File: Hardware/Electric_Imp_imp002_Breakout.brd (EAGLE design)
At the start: 43.2 x 45.7 mm, 41 parts, among them Q1 DMG2307L-7, Q2 PHOTOTRANSISTORPT17-21C-L41-T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, U1 imp002, U2 TPS62172, X1 USBSMD

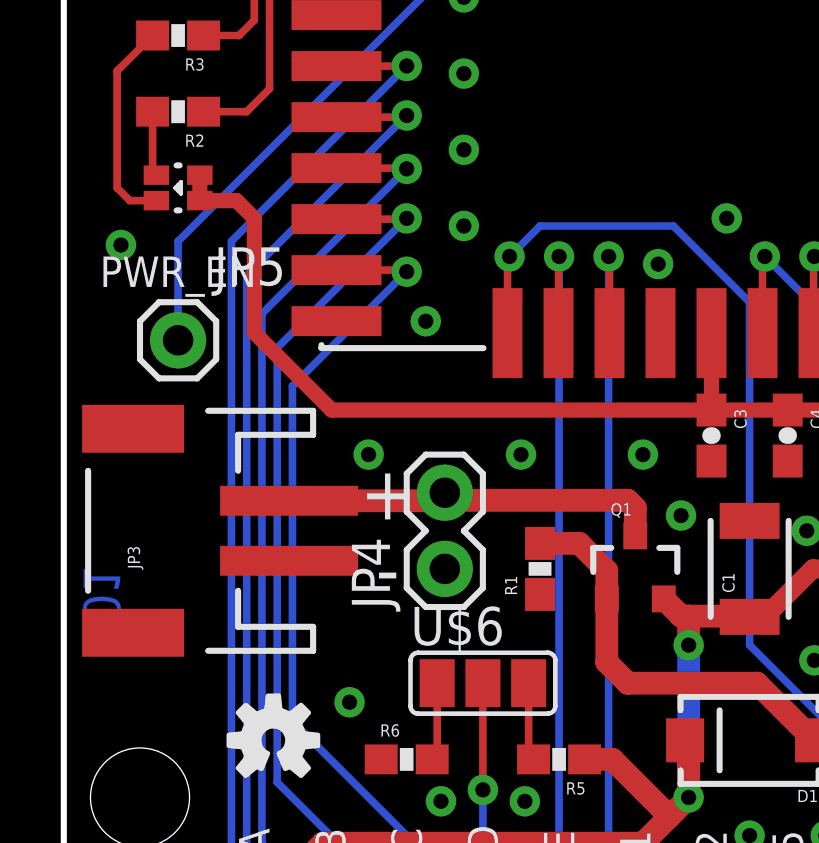
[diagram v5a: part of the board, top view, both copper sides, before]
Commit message: Added silk to the 3-way jumper, moved marking for dual-color diode to outside footprint, and changed phototransistor gain resistor to 33k
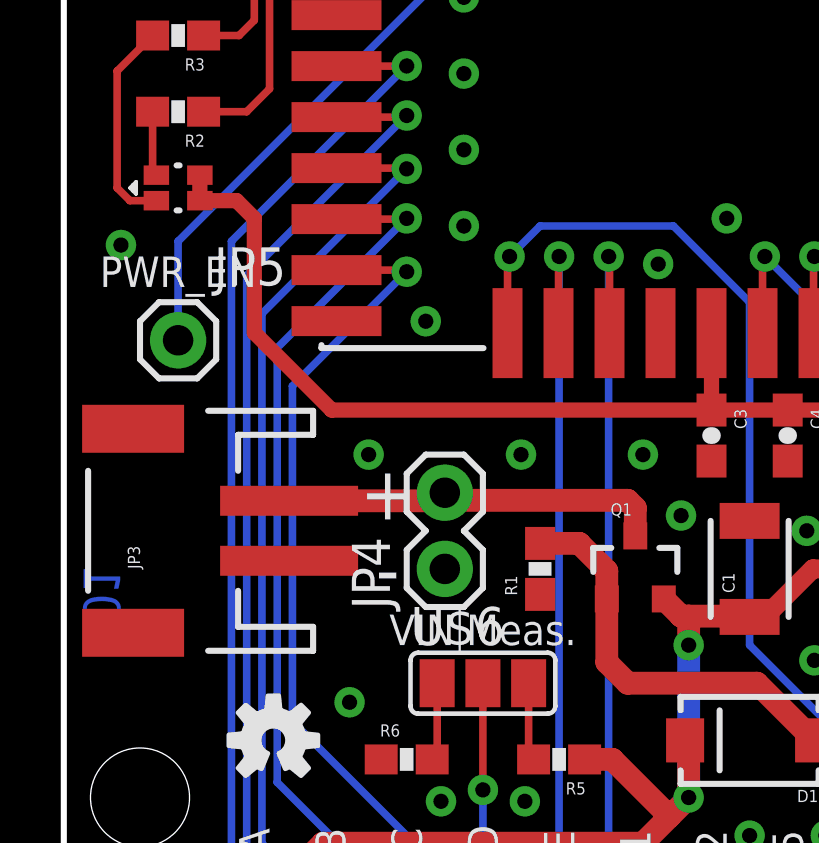
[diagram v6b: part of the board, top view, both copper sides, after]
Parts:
- R4: value 62k -> 33k
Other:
- board text added: "VIN Meas."
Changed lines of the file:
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@@
 <setting verticaltext="up"/>
 </settings>
-<grid distance="0.05" unitdist="inch" unit="inch" style="dots" multiple="1" display="yes" altdistance="0.005" altunitdist="inch" altunit="inch"/>
+<grid distance="0.01" unitdist="inch" unit="inch" style="dots" multiple="1" display="yes" altdistance="0.005" altunitdist="inch" altunit="inch"/>
 <layers>
 <layer number="1" name="Top" color="4" fill="1" visible="yes" active="yes"/>
 <layer number="2" name="Route2" color="1" fill="3" visible="no" active="yes"/>
 <layer number="15" name="Route15" color="4" fill="6" visible="no" active="yes"/>
-<layer number="16" name="Bottom" color="1" fill="1" visible="yes" active="yes"/>
+<layer number="16" name="Bottom" color="1" fill="1" visible="no" active="yes"/>
 <layer number="17" name="Pads" color="2" fill="1" visible="yes" active="yes"/>
 <layer number="18" name="Vias" color="2" fill="1" visible="yes" active="yes"/>
@@
 <layer number="20" name="Dimension" color="15" fill="1" visible="yes" active="yes"/>
 <layer number="21" name="tPlace" color="16" fill="1" visible="yes" active="yes"/>
-<layer number="22" name="bPlace" color="14" fill="1" visible="yes" active="yes"/>
+<layer number="22" name="bPlace" color="14" fill="1" visible="no" active="yes"/>
 <layer number="23" name="tOrigins" color="15" fill="1" visible="yes" active="yes"/>
-<layer number="24" name="bOrigins" color="15" fill="1" visible="yes" active="yes"/>
+<layer number="24" name="bOrigins" color="15" fill="1" visible="no" active="yes"/>
 <layer number="25" name="tNames" color="7" fill="1" visible="no" active="yes"/>
 <layer number="26" name="bNames" color="7" fill="1" visible="no" active="yes"/>
@@
 <layer number="43" name="vRestrict" color="2" fill="10" visible="no" active="yes"/>
 <layer number="44" name="Drills" color="7" fill="1" visible="no" active="yes"/>
-<layer number="45" name="Holes" color="7" fill="1" visible="yes" active="yes"/>
+<layer number="45" name="Holes" color="7" fill="1" visible="no" active="yes"/>
 <layer number="46" name="Milling" color="3" fill="1" visible="no" active="yes"/>
-<layer number="51" name="tDocu" color="6" fill="1" visible="yes" active="yes"/>
+<layer number="51" name="tDocu" color="6" fill="1" visible="no" active="yes"/>
 <layer number="52" name="bDocu" color="7" fill="1" visible="no" active="yes"/>
 <layer number="3" name="Route3" color="4" fill="3" visible="no" active="no"/>
@@
 <text x="10.795" y="16.891" size="1.778" layer="21" font="vector" ratio="15" align="bottom-center">+</text>
 <text x="10.795" y="14.351" size="1.778" layer="21" font="vector" ratio="15" align="bottom-center">-</text>
+<text x="13.97" y="12.7" size="1.016" layer="21" font="vector" ratio="15" align="bottom-center">VIN Meas.</text>
 </plain>
 <attributes>
@@
 <attribute name="PROD_ID" value="RES-00818" x="3.81" y="33.02" size="1.778" layer="27" font="vector" ratio="15" rot="R180" display="off"/>
 </element>
-<element name="R4" library="SparkFun-Resistors" package="0603-RES" value="62k" x="3.81" y="35.56" rot="R180"/>
+<element name="R4" library="SparkFun-Resistors" package="0603-RES" value="33k" x="3.81" y="35.56" rot="R180"/>
 <element name="JP1" library="SparkFun-Connectors" package="1X15" value="M15" x="41.91" y="1.27" rot="R180"/>
 <element name="JP5" library="SparkFun-Connectors" package="1X01" value="M01PTH" x="3.81" y="22.86"/>

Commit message: Changed rev number to v10
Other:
- board text added: "v10"
- board text removed: "v01"
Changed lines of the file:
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@@
 <setting verticaltext="up"/>
 </settings>
-<grid distance="0.01" unitdist="inch" unit="inch" style="dots" multiple="1" display="yes" altdistance="0.005" altunitdist="inch" altunit="inch"/>
+<grid distance="0.05" unitdist="inch" unit="inch" style="dots" multiple="1" display="yes" altdistance="0.005" altunitdist="inch" altunit="inch"/>
 <layers>
 <layer number="1" name="Top" color="4" fill="1" visible="yes" active="yes"/>
 <layer number="2" name="Route2" color="1" fill="3" visible="no" active="yes"/>
 <layer number="15" name="Route15" color="4" fill="6" visible="no" active="yes"/>
-<layer number="16" name="Bottom" color="1" fill="1" visible="no" active="yes"/>
+<layer number="16" name="Bottom" color="1" fill="1" visible="yes" active="yes"/>
 <layer number="17" name="Pads" color="2" fill="1" visible="yes" active="yes"/>
 <layer number="18" name="Vias" color="2" fill="1" visible="yes" active="yes"/>
@@
 <layer number="20" name="Dimension" color="15" fill="1" visible="yes" active="yes"/>
 <layer number="21" name="tPlace" color="16" fill="1" visible="yes" active="yes"/>
-<layer number="22" name="bPlace" color="14" fill="1" visible="no" active="yes"/>
+<layer number="22" name="bPlace" color="14" fill="1" visible="yes" active="yes"/>
 <layer number="23" name="tOrigins" color="15" fill="1" visible="yes" active="yes"/>
-<layer number="24" name="bOrigins" color="15" fill="1" visible="no" active="yes"/>
+<layer number="24" name="bOrigins" color="15" fill="1" visible="yes" active="yes"/>
 <layer number="25" name="tNames" color="7" fill="1" visible="no" active="yes"/>
 <layer number="26" name="bNames" color="7" fill="1" visible="no" active="yes"/>
@@
 <layer number="43" name="vRestrict" color="2" fill="10" visible="no" active="yes"/>
 <layer number="44" name="Drills" color="7" fill="1" visible="no" active="yes"/>
-<layer number="45" name="Holes" color="7" fill="1" visible="no" active="yes"/>
+<layer number="45" name="Holes" color="7" fill="1" visible="yes" active="yes"/>
 <layer number="46" name="Milling" color="3" fill="1" visible="no" active="yes"/>
-<layer number="51" name="tDocu" color="6" fill="1" visible="no" active="yes"/>
+<layer number="51" name="tDocu" color="6" fill="1" visible="yes" active="yes"/>
 <layer number="52" name="bDocu" color="7" fill="1" visible="no" active="yes"/>
 <layer number="3" name="Route3" color="4" fill="3" visible="no" active="no"/>
@@
 <rectangle x1="24.748365625" y1="41.557321875" x2="24.769446875" y2="41.567734375" layer="22" rot="R180"/>
 <rectangle x1="18.2673" y1="41.557321875" x2="18.28838125" y2="41.567734375" layer="22" rot="R180"/>
-<text x="1.27" y="13.97" size="1.2192" layer="16" font="vector" ratio="15" rot="MR270" align="center">v01</text>
+<text x="1.27" y="13.97" size="1.2192" layer="16" font="vector" ratio="15" rot="MR270" align="center">v10</text>
 <text x="21.59" y="10.922" size="1.778" layer="22" font="vector" ratio="15" rot="MR0" align="center">imp002 Breakout</text>
 <text x="21.59" y="8.89" size="0.8128" layer="22" font="vector" ratio="15" rot="MR0" align="center">VIN = 3.3 - 17V</text>

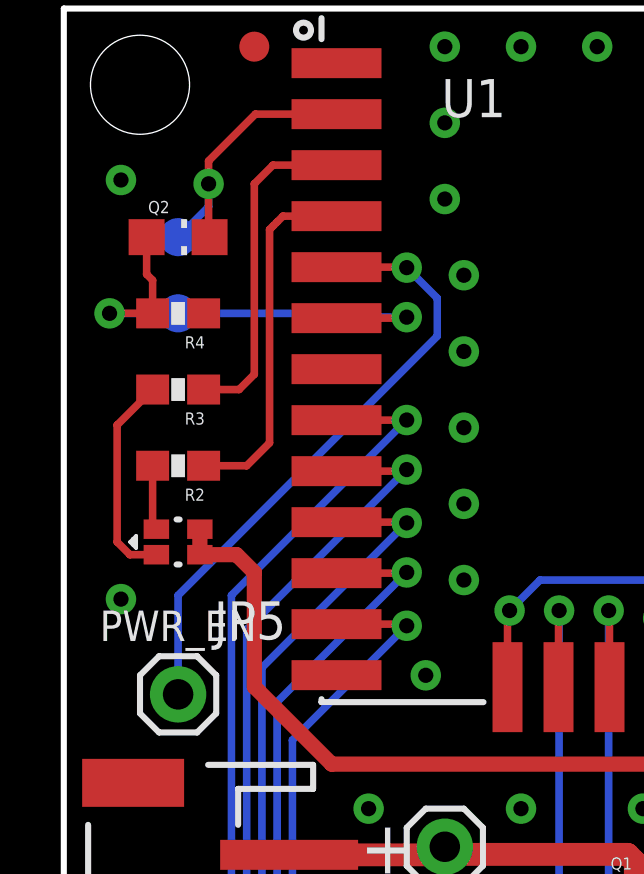
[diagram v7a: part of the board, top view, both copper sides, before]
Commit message: Added 10k pullup on LED_R line. Added warning notes to the solder jumpers.
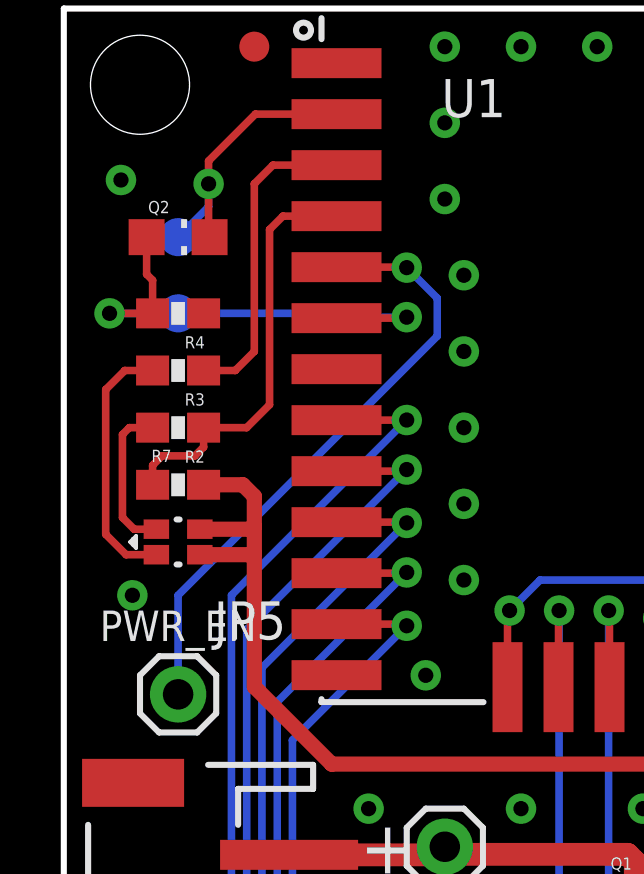
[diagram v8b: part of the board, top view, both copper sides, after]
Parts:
- added R7: 10K, SparkFun-Resistors:0603-RES
- moved R2 1.27 mm to (3.81, 31.8)
- moved R3 0.63 mm to (3.81, 33.7)
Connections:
- net 3.3V: now also R7.2
- net LED_R: now also R7.1
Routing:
- net 3.3V: track 93.5 -> 98.7 mm
- net N$4: track 2.17 -> 5.16 mm
- net LED_R: track 12.0 -> 14.0 mm
- net N$5: track 7.05 -> 8.62 mm
- net LED_G: track 11.2 -> 10.5 mm
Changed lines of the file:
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@@
 <setting verticaltext="up"/>
 </settings>
-<grid distance="0.05" unitdist="inch" unit="inch" style="dots" multiple="1" display="yes" altdistance="0.005" altunitdist="inch" altunit="inch"/>
+<grid distance="0.05" unitdist="inch" unit="inch" style="dots" multiple="1" display="yes" altdistance="0.025" altunitdist="inch" altunit="inch"/>
 <layers>
 <layer number="1" name="Top" color="4" fill="1" visible="yes" active="yes"/>
@@
 <attribute name="PROD_ID" value="DIO-12140" x="3.81" y="27.94" size="1.778" layer="27" font="vector" ratio="15" rot="R270" display="off"/>
 </element>
-<element name="R2" library="SparkFun-Resistors" package="0603-RES" value="330" x="3.81" y="30.48" rot="R180">
-<attribute name="PROD_ID" value="RES-00818" x="3.81" y="30.48" size="1.778" layer="27" font="vector" ratio="15" rot="R180" display="off"/>
+<element name="R2" library="SparkFun-Resistors" package="0603-RES" value="330" x="3.81" y="31.75" rot="R180">
+<attribute name="PROD_ID" value="RES-00818" x="3.81" y="31.75" size="1.778" layer="27" font="vector" ratio="15" rot="R180" display="off"/>
 </element>
-<element name="R3" library="SparkFun-Resistors" package="0603-RES" value="330" x="3.81" y="33.02" rot="R180">
-<attribute name="PROD_ID" value="RES-00818" x="3.81" y="33.02" size="1.778" layer="27" font="vector" ratio="15" rot="R180" display="off"/>
+<element name="R3" library="SparkFun-Resistors" package="0603-RES" value="330" x="3.81" y="33.655" rot="R180">
+<attribute name="PROD_ID" value="RES-00818" x="3.81" y="33.655" size="1.778" layer="27" font="vector" ratio="15" rot="R180" display="off"/>
 </element>
 <element name="R4" library="SparkFun-Resistors" package="0603-RES" value="33k" x="3.81" y="35.56" rot="R180"/>
@@
 <element name="LOGO1" library="SparkFun-Aesthetics" package="OSHW-LOGO-S" value="OSHW-LOGOS" x="6.985" y="9.525"/>
 <element name="LOGO2" library="SparkFun-Aesthetics" package="SFE_LOGO_FLAME_.1" value="SFE_LOGO_FLAME.1_INCH" x="31.115" y="8.255"/>
+<element name="R7" library="SparkFun-Resistors" package="0603-RES" value="10K" x="3.81" y="29.845">
+<attribute name="PROD_ID" value="RES-00824" x="3.81" y="29.845" size="1.778" layer="27" font="vector" ratio="15" display="off"/>
+</element>
 </elements>
 <signals>
@@
 <via x="12.065" y="23.495" extent="1-16" drill="0.508"/>
 <via x="1.905" y="40.005" extent="1-16" drill="0.508"/>
-<via x="1.905" y="26.035" extent="1-16" drill="0.508"/>
+<via x="2.286" y="26.162" extent="1-16" drill="0.508"/>
 <via x="15.24" y="19.05" extent="1-16" drill="0.508"/>
 <via x="10.16" y="19.05" extent="1-16" drill="0.508"/>
@@
 <wire x1="38.52" y1="27.94" x2="37.338" y2="27.94" width="0.508" layer="1"/>
 <wire x1="38.9573" y1="33.02" x2="37.338" y2="33.02" width="0.508" layer="1"/>
-<wire x1="4.535" y1="27.515" x2="5.759" y2="27.515" width="0.508" layer="1"/>
-<wire x1="5.759" y1="27.515" x2="6.35" y2="26.924" width="0.508" layer="1"/>
-<wire x1="6.35" y1="26.924" x2="6.35" y2="23.114" width="0.508" layer="1"/>
-<wire x1="4.535" y1="27.515" x2="4.535" y2="28.365" width="0.508" layer="1"/>
+<wire x1="6.35" y1="29.464" x2="6.35" y2="28.448" width="0.508" layer="1"/>
+<wire x1="6.35" y1="28.448" x2="6.35" y2="27.559" width="0.508" layer="1"/>
+<wire x1="6.35" y1="27.559" x2="6.35" y2="23.114" width="0.508" layer="1"/>
 <wire x1="34.544" y1="6.096" x2="32.512" y2="6.096" width="0.508" layer="1"/>
 <wire x1="32.512" y1="6.096" x2="28.702" y2="9.906" width="0.508" layer="1"/>
@@
 <wire x1="8.929" y1="20.535" x2="6.35" y2="23.114" width="0.508" layer="1"/>
 <wire x1="21.59" y1="23.1" x2="21.59" y2="20.535" width="0.508" layer="1"/>
+<contactref element="R7" pad="2"/>
+<wire x1="4.66" y1="29.845" x2="5.969" y2="29.845" width="0.508" layer="1"/>
+<wire x1="5.969" y1="29.845" x2="6.35" y2="29.464" width="0.508" layer="1"/>
+<wire x1="4.535" y1="27.515" x2="6.306" y2="27.515" width="0.508" layer="1"/>
+<wire x1="6.306" y1="27.515" x2="6.35" y2="27.559" width="0.508" layer="1"/>
+<wire x1="4.535" y1="28.365" x2="6.267" y2="28.365" width="0.508" layer="1"/>
+<wire x1="6.267" y1="28.365" x2="6.35" y2="28.448" width="0.508" layer="1"/>
 </signal>
 <signal name="VIN">
@@
 <contactref element="D2" pad="P$4"/>
 <contactref element="R2" pad="2"/>
-<wire x1="2.96" y1="30.48" x2="2.96" y2="28.49" width="0.254" layer="1"/>
-<wire x1="2.96" y1="28.49" x2="3.085" y2="28.365" width="0.254" layer="1"/>
+<wire x1="3.085" y1="28.365" x2="2.3436" y2="28.365" width="0.254" layer="1"/>
+<wire x1="2.3436" y1="28.365" x2="1.9558" y2="28.7528" width="0.254" layer="1"/>
+<wire x1="2.96" y1="31.75" x2="2.1844" y2="31.75" width="0.254" layer="1"/>
+<wire x1="2.1844" y1="31.75" x2="1.9558" y2="31.5214" width="0.254" layer="1"/>
+<wire x1="1.9558" y1="31.5214" x2="1.9558" y2="28.7528" width="0.254" layer="1"/>
 </signal>
 <signal name="N$5">
 <contactref element="D2" pad="P$3"/>
 <contactref element="R3" pad="2"/>
-<wire x1="3.085" y1="27.515" x2="2.203" y2="27.515" width="0.254" layer="1"/>
-<wire x1="2.203" y1="27.515" x2="1.778" y2="27.94" width="0.254" layer="1"/>
-<wire x1="1.778" y1="27.94" x2="1.778" y2="31.838" width="0.254" layer="1"/>
-<wire x1="1.778" y1="31.838" x2="2.96" y2="33.02" width="0.254" layer="1"/>
+<wire x1="2.96" y1="33.655" x2="2.032" y2="33.655" width="0.254" layer="1"/>
+<wire x1="2.032" y1="33.655" x2="1.397" y2="33.02" width="0.254" layer="1"/>
+<wire x1="3.085" y1="27.515" x2="2.076" y2="27.515" width="0.254" layer="1"/>
+<wire x1="2.076" y1="27.515" x2="1.397" y2="28.194" width="0.254" layer="1"/>
+<wire x1="1.397" y1="28.194" x2="1.397" y2="33.02" width="0.254" layer="1"/>
 </signal>
 <signal name="LED_R">
 <contactref element="U1" pad="4"/>
 <contactref element="R2" pad="1"/>
-<wire x1="4.66" y1="30.48" x2="6.096" y2="30.48" width="0.254" layer="1"/>
-<wire x1="6.096" y1="30.48" x2="6.858" y2="31.242" width="0.254" layer="1"/>
-<wire x1="6.858" y1="31.242" x2="6.858" y2="38.354" width="0.254" layer="1"/>
-<wire x1="6.858" y1="38.354" x2="6.985" y2="38.481" width="0.254" layer="1"/>
-<wire x1="6.985" y1="38.481" x2="7.112" y2="38.608" width="0.254" layer="1"/>
 <wire x1="9.09" y1="38.8" x2="7.304" y2="38.8" width="0.254" layer="1"/>
-<wire x1="7.304" y1="38.8" x2="7.112" y2="38.608" width="0.254" layer="1"/>
+<wire x1="7.304" y1="38.8" x2="6.858" y2="38.354" width="0.254" layer="1"/>
+<contactref element="R7" pad="1"/>
+<wire x1="4.66" y1="31.75" x2="6.096" y2="31.75" width="0.254" layer="1"/>
+<wire x1="6.096" y1="31.75" x2="6.858" y2="32.512" width="0.254" layer="1"/>
+<wire x1="6.858" y1="32.512" x2="6.858" y2="38.354" width="0.254" layer="1"/>
+<wire x1="2.96" y1="29.845" x2="2.96" y2="30.4936" width="0.254" layer="1"/>
+<wire x1="2.96" y1="30.4936" x2="3.2766" y2="30.8102" width="0.254" layer="1"/>
+<wire x1="4.66" y1="31.75" x2="4.66" y2="31.1014" width="0.254" layer="1"/>
+<wire x1="4.66" y1="31.1014" x2="4.3688" y2="30.8102" width="0.254" layer="1"/>
+<wire x1="4.3688" y1="30.8102" x2="3.2766" y2="30.8102" width="0.254" layer="1"/>
 </signal>
 <signal name="LED_G">
 <contactref element="U1" pad="3"/>
 <contactref element="R3" pad="1"/>
-<wire x1="4.66" y1="33.02" x2="5.842" y2="33.02" width="0.254" layer="1"/>
-<wire x1="5.842" y1="33.02" x2="6.35" y2="33.528" width="0.254" layer="1"/>
-<wire x1="6.35" y1="33.528" x2="6.35" y2="39.878" width="0.254" layer="1"/>
 <wire x1="6.35" y1="39.878" x2="6.972" y2="40.5" width="0.254" layer="1"/>
 <wire x1="9.09" y1="40.5" x2="6.972" y2="40.5" width="0.254" layer="1"/>
+<wire x1="4.66" y1="33.655" x2="5.715" y2="33.655" width="0.254" layer="1"/>
+<wire x1="5.715" y1="33.655" x2="6.35" y2="34.29" width="0.254" layer="1"/>
+<wire x1="6.35" y1="34.29" x2="6.35" y2="39.878" width="0.254" layer="1"/>
 </signal>
 <signal name="OPTO_BIAS">
@@
 </signal>
 </signals>
+<errors>
+</errors>
 </board>
 </drawing>
